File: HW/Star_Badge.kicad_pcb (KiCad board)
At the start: 2 copper layers, 180 x 171.6 mm, 55 parts, among them J1 AVR-ISP-6, J2 10118194-0001LF, Q1 Q_NMOS_DGS, Q2 Q_PMOS_DGS, U1 ATTINY861-15XD, U2 TPS613221ADBVT, U3 AP7363-33D-13, X1 Badgelife_sao_connector_v169b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, X2 Badgelife_sao_connector_v169b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, X3 Badgelife_sao_connector_v169b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

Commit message: update layout with new test points
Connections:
- TP3 pad 1: /R_LED_BUS -> /R_PWM__MISO
- TP4 pad 1: /G_LED_BUS -> /G_PWM
- TP5 pad 1: /B_LED_BUS -> /B_PWM
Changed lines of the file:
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@@
   )
   (setup
-    (last_trace_width 0.508)
+    (last_trace_width 0.1524)
     (user_trace_width 0.1524)
     (user_trace_width 0.2032)
@@
     )
     (pad 1 smd circle (at 0 0) (size 1 1) (layers B.Cu B.Mask)
-      (net 6 /R_LED_BUS))
+      (net 14 /R_PWM__MISO))
   )
   (module TestPoint:TestPoint_Pad_D1.0mm (layer B.Cu)
@@
     (fp_circle (center 0 0) (end 0 -0.7) (layer B.SilkS) (width 0.12))
     (pad 1 smd circle (at 0 0) (size 1 1) (layers B.Cu B.Mask)
-      (net 8 /G_LED_BUS))
+      (net 21 /G_PWM))
   )
   (module TestPoint:TestPoint_Pad_D1.0mm (layer B.Cu)
@@
     )
     (pad 1 smd circle (at 0 0) (size 1 1) (layers B.Cu B.Mask)
-      (net 9 /B_LED_BUS))
+      (net 22 /B_PWM))
   )
   (module TestPoint:TestPoint_Pad_D1.0mm (layer B.Cu)

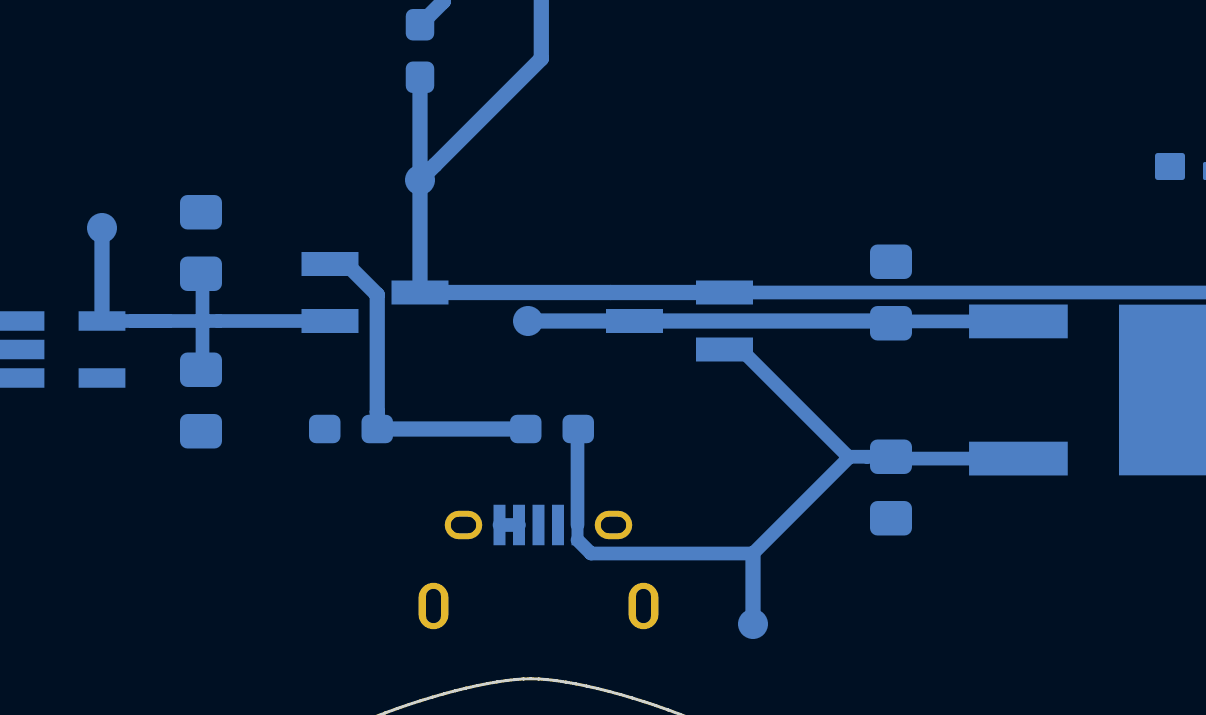
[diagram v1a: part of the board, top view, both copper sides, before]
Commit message: Spaced out parts
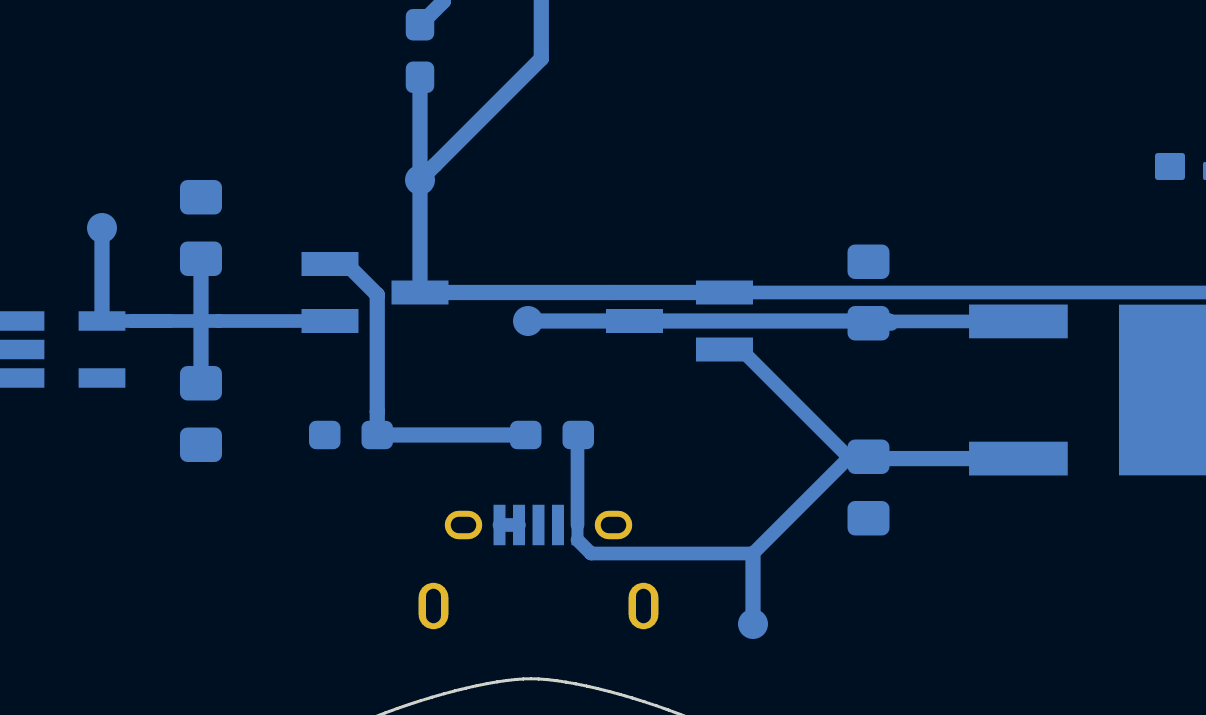
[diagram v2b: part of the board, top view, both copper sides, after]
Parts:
- moved C1 0.75 mm to (111.2, 154.2)
- moved C2 0.75 mm to (111.2, 147.8)
- moved C3 0.50 mm to (89.0, 145.6)
- moved C4 0.45 mm to (89.0, 151.8)
- moved R6 0.20 mm to (100.7, 152.5)
- moved R7 0.20 mm to (94.0, 152.5)
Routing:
- net /V_BAT: track 15.2 -> 16.2 mm
- net /V_USB: track 27.3 -> 28.0 mm
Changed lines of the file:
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@@
     (thickness 1.6)
     (drawings 611)
-    (tracks 62)
+    (tracks 58)
     (zones 0)
     (modules 55)
@@
   (page A4)
   (layers
-    (0 F.Cu signal)
+    (0 F.Cu signal hide)
     (31 B.Cu signal)
     (32 B.Adhes user hide)
@@
     (35 F.Paste user hide)
     (36 B.SilkS user)
-    (37 F.SilkS user)
+    (37 F.SilkS user hide)
     (38 B.Mask user)
     (39 F.Mask user hide)
@@
     (44 Edge.Cuts user)
     (45 Margin user hide)
-    (46 B.CrtYd user)
+    (46 B.CrtYd user hide)
     (47 F.CrtYd user hide)
     (48 B.Fab user hide)
@@
   )
   (setup
-    (last_trace_width 0.1524)
+    (last_trace_width 0.508)
     (user_trace_width 0.1524)
     (user_trace_width 0.2032)
@@
       (effects (font (size 1 1) (thickness 0.15)) (justify mirror))
     )
-    (fp_text value AP7363-33D-13 (at 1.289178 -6.901489 180) (layer B.SilkS) hide
+    (fp_text value AP7363-33D-13 (at -4.2 -0.1 180) (layer B.SilkS) hide
       (effects (font (size 1 1) (thickness 0.15)) (justify mirror))
     )
@@
   )
   (module Resistor_SMD:R_0603_1608Metric_Pad1.05x0.95mm_HandSolder (layer B.Cu)
-    (at 94 152.3)
+    (at 94 152.5)
     (descr "Resistor SMD 0603 (1608 Metric), square (rectangular) end terminal, IPC_7351 nominal with elongated pad for handsoldering. (Body size source: http://www.tortai-tech.com/upload/download/2011102023233369053.pdf), generated with kicad-footprint-generator")
     (tags "resistor handsolder")
@@
   )
   (module Resistor_SMD:R_0603_1608Metric_Pad1.05x0.95mm_HandSolder (layer B.Cu)
-    (at 100.7 152.3)
+    (at 100.7 152.5)
     (descr "Resistor SMD 0603 (1608 Metric), square (rectangular) end terminal, IPC_7351 nominal with elongated pad for handsoldering. (Body size source: http://www.tortai-tech.com/upload/download/2011102023233369053.pdf), generated with kicad-footprint-generator")
     (tags "resistor handsolder")
@@
   )
   (module Capacitor_SMD:C_0805_2012Metric_Pad1.15x1.40mm_HandSolder (layer B.Cu)
-    (at 89 151.35 270)
+    (at 89 151.8 270)
     (descr "Capacitor SMD 0805 (2012 Metric), square (rectangular) end terminal, IPC_7351 nominal with elongated pad for handsoldering. (Body size source: https://docs.google.com/spreadsheets/d/1BsfQQcO9C6DZCsRaXUlFlo91Tg2WpOkGARC1WS5S8t0/edit?usp=sharing), generated with kicad-footprint-generator")
     (tags "capacitor handsolder")
@@
   )
   (module Capacitor_SMD:C_0805_2012Metric_Pad1.15x1.40mm_HandSolder (layer B.Cu)
-    (at 89 146.1 90)
+    (at 89 145.6 90)
     (descr "Capacitor SMD 0805 (2012 Metric), square (rectangular) end terminal, IPC_7351 nominal with elongated pad for handsoldering. (Body size source: https://docs.google.com/spreadsheets/d/1BsfQQcO9C6DZCsRaXUlFlo91Tg2WpOkGARC1WS5S8t0/edit?usp=sharing), generated with kicad-footprint-generator")
     (tags "capacitor handsolder")
@@
   )
   (module Capacitor_SMD:C_0805_2012Metric_Pad1.15x1.40mm_HandSolder (layer B.Cu)
-    (at 112 147.75 90)
+    (at 111.25 147.75 90)
     (descr "Capacitor SMD 0805 (2012 Metric), square (rectangular) end terminal, IPC_7351 nominal with elongated pad for handsoldering. (Body size source: https://docs.google.com/spreadsheets/d/1BsfQQcO9C6DZCsRaXUlFlo91Tg2WpOkGARC1WS5S8t0/edit?usp=sharing), generated with kicad-footprint-generator")
     (tags "capacitor handsolder")
@@
   )
   (module Capacitor_SMD:C_0805_2012Metric_Pad1.15x1.40mm_HandSolder (layer B.Cu)
-    (at 112 154.25 270)
+    (at 111.25 154.25 270)
     (descr "Capacitor SMD 0805 (2012 Metric), square (rectangular) end terminal, IPC_7351 nominal with elongated pad for handsoldering. (Body size source: https://docs.google.com/spreadsheets/d/1BsfQQcO9C6DZCsRaXUlFlo91Tg2WpOkGARC1WS5S8t0/edit?usp=sharing), generated with kicad-footprint-generator")
     (tags "capacitor handsolder")
@@
   (gr_line (start 100.038258 14.223787) (end 100.038258 14.223787) (layer Edge.Cuts) (width 0.1))
   (segment (start 99.6 155.5) (end 98.95 155.5) (width 0.4572) (layer B.Cu) (net 1))
-  (segment (start 89.075 152.3) (end 89 152.375) (width 0.508) (layer B.Cu) (net 1))
   (segment (start 72.85 116.475) (end 66.6 124.1822) (width 0.4572) (layer B.Cu) (net 2))
   (segment (start 79.05 148.5) (end 79.2 148.65) (width 0.4572) (layer B.Cu) (net 2))
@@
   (segment (start 73.2 148.55) (end 73.2 151.5) (width 0.508) (layer B.Cu) (net 2))
   (segment (start 73.25 148.5) (end 73.2 148.55) (width 0.508) (layer B.Cu) (net 2))
-  (segment (start 112.211 153.286) (end 112.15 153.225) (width 0.4572) (layer B.Cu) (net 3))
-  (segment (start 116.2468 153.286) (end 112.211 153.286) (width 0.4572) (layer B.Cu) (net 3))
-  (segment (start 111.2 153.225) (end 112 153.225) (width 0.4572) (layer B.Cu) (net 3))
   (segment (start 107.4 156.45) (end 110.625 153.225) (width 0.4572) (layer B.Cu) (net 3))
   (segment (start 101.55 156) (end 102 156.45) (width 0.4572) (layer B.Cu) (net 3))
@@
   (segment (start 110.625 153.225) (end 110.575 153.225) (width 0.4572) (layer B.Cu) (net 3))
   (segment (start 107.4 158.8) (end 107.4 156.45) (width 0.508) (layer B.Cu) (net 3))
+  (segment (start 110.686 153.286) (end 110.625 153.225) (width 0.508) (layer B.Cu) (net 3))
+  (segment (start 116.2468 153.286) (end 110.686 153.286) (width 0.508) (layer B.Cu) (net 3))
   (segment (start 112.011 148.714) (end 112 148.725) (width 0.4572) (layer B.Cu) (net 4))
   (segment (start 116.2468 148.714) (end 112.011 148.714) (width 0.4572) (layer B.Cu) (net 4))
@@
   (segment (start 89.5872 148.7) (end 93.3 148.7) (width 0.4572) (layer B.Cu) (net 5))
   (segment (start 86.7 148.7) (end 87.9372 148.7) (width 0.4572) (layer B.Cu) (net 5))
-  (segment (start 89 150.275) (end 89.05 150.325) (width 0.4572) (layer B.Cu) (net 5))
-  (segment (start 89.05 148.65) (end 89.05 147.125) (width 0.4572) (layer B.Cu) (net 5))
   (segment (start 89.05 148.7) (end 89 148.65) (width 0.4572) (layer B.Cu) (net 5))
   (segment (start 89.5872 148.7) (end 89.05 148.7) (width 0.4572) (layer B.Cu) (net 5))
   (segment (start 89.05 148.7) (end 85.7 148.7) (width 0.4572) (layer B.Cu) (net 5))
-  (segment (start 89.05 148.7) (end 89.05 150.325) (width 0.4572) (layer B.Cu) (net 5))
   (segment (start 85.7 148.7) (end 85.7 145.6) (width 0.508) (layer B.Cu) (net 5))
+  (segment (start 89 150.775) (end 89 146.625) (width 0.508) (layer B.Cu) (net 5))
   (segment (start 102.6572 147.75) (end 106.45 147.75) (width 0.508) (layer B.Cu) (net 15))
   (segment (start 102.6572 147.75) (end 96.3 147.75) (width 0.508) (layer B.Cu) (net 15))
@@
   (segment (start 83 150.6) (end 79.225 150.6) (width 0.4572) (layer B.Cu) (net 19))
   (segment (start 93.3 146.8) (end 93.314198 146.8) (width 0.4572) (layer B.Cu) (net 20))
-  (segment (start 94.875 152.3) (end 99.825 152.3) (width 0.508) (layer B.Cu) (net 20))
+  (segment (start 94.875 152.5) (end 99.825 152.5) (width 0.508) (layer B.Cu) (net 20))
   (segment (start 94.875 147.825) (end 94.875 151.725) (width 0.508) (layer B.Cu) (net 20))
   (segment (start 93.85 146.8) (end 94.875 147.825) (width 0.508) (layer B.Cu) (net 20))

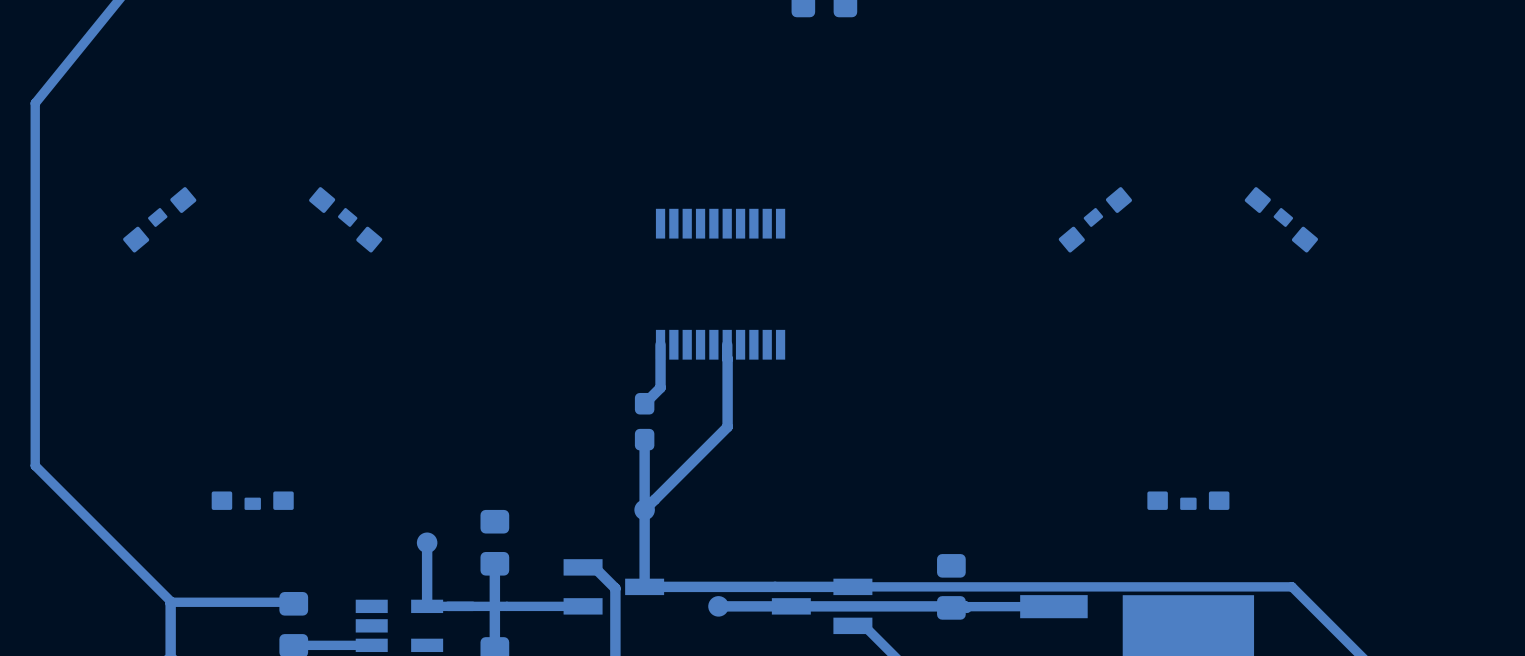
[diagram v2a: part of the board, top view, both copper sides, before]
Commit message: Routing - net around star 3. Adjusted R G LED to route.
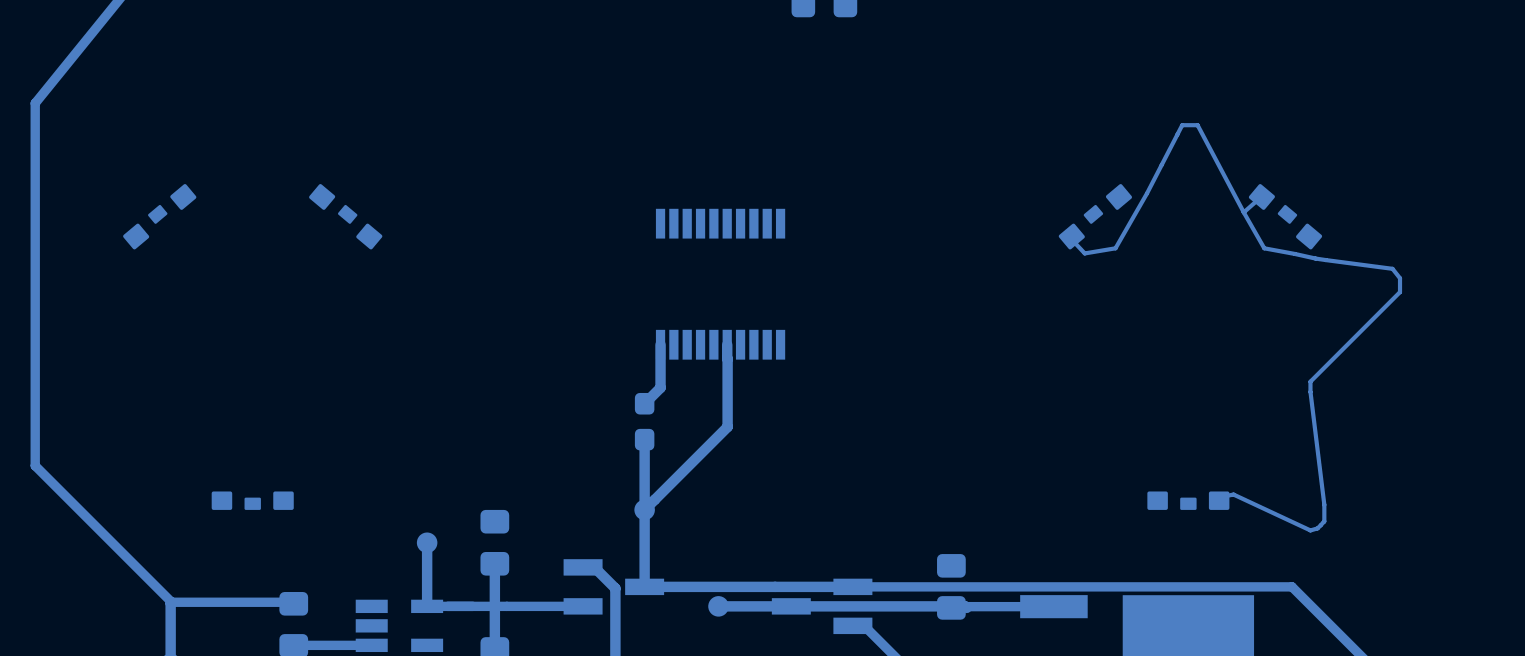
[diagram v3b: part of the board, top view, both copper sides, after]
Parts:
- moved D10 0.25 mm to (127.5, 129.8)
- moved D11 0.15 mm to (118.3, 129.8)
- moved D7 0.15 mm to (81.7, 129.8)
- moved D8 0.15 mm to (72.7, 129.8)
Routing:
- net /EN_RGB3: track 0.00 -> 44.1 mm
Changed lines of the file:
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@@
     (thickness 1.6)
     (drawings 611)
-    (tracks 58)
+    (tracks 85)
     (zones 0)
     (modules 55)
@@
     (32 B.Adhes user hide)
     (33 F.Adhes user hide)
-    (34 B.Paste user)
+    (34 B.Paste user hide)
     (35 F.Paste user hide)
     (36 B.SilkS user)
@@
   )
   (setup
-    (last_trace_width 0.508)
+    (last_trace_width 0.2032)
     (user_trace_width 0.1524)
     (user_trace_width 0.2032)
@@
   )
   (module Star_Badge:1204_SIDE_VIEW_LED locked (layer B.Cu)
-    (at 118.3 129.9 40)
+    (at 118.3 129.75 40)
     (fp_text reference D11 (at -0.031676 -1.984691 40) (layer B.SilkS)
       (effects (font (size 0.7 0.7) (thickness 0.15)) (justify mirror))
@@
   )
   (module Star_Badge:1204_SIDE_VIEW_LED locked (layer B.Cu)
-    (at 127.3 129.9 320)
+    (at 127.5 129.75 320)
     (fp_text reference D10 (at 0.044002 -2.125574 320) (layer B.SilkS)
       (effects (font (size 0.7 0.7) (thickness 0.15)) (justify mirror))
@@
     )
   )
-  (module Star_Badge:1204_SIDE_VIEW_LED (layer B.Cu)
-    (at 72.7 129.9 40)
+  (module Star_Badge:1204_SIDE_VIEW_LED locked (layer B.Cu)
+    (at 72.7 129.75 40)
     (fp_text reference D8 (at 0.084555 -2.278783 40) (layer B.SilkS)
       (effects (font (size 0.7 0.7) (thickness 0.15)) (justify mirror))
@@
     )
   )
-  (module Star_Badge:1204_SIDE_VIEW_LED (layer B.Cu)
-    (at 81.7 129.9 320)
+  (module Star_Badge:1204_SIDE_VIEW_LED locked (layer B.Cu)
+    (at 81.7 129.75 320)
     (fp_text reference D7 (at 0.044002 -2.125574 320) (layer B.SilkS)
       (effects (font (size 0.7 0.7) (thickness 0.15)) (justify mirror))
@@
   (segment (start 85.7 148.7) (end 85.7 145.6) (width 0.508) (layer B.Cu) (net 5))
   (segment (start 89 150.775) (end 89 146.625) (width 0.508) (layer B.Cu) (net 5))
+  (segment (start 119.25 131.25) (end 117.75 131.5) (width 0.2032) (layer B.Cu) (net 12))
+  (segment (start 121.5 127.186948) (end 120.78461 128.573568) (width 0.2032) (layer B.Cu) (net 12))
+  (segment (start 117.75 131.5) (end 117.118794 130.825879) (width 0.2032) (layer B.Cu) (net 12))
+  (segment (start 120.78461 128.573568) (end 119.25 131.25) (width 0.2032) (layer B.Cu) (net 12))
+  (segment (start 125.5 129.5) (end 123.25 125.25) (width 0.2032) (layer B.Cu) (net 12))
+  (segment (start 126.183073 128.897516) (end 125.5 129.5) (width 0.2032) (layer B.Cu) (net 12))
+  (segment (start 123.25 125.25) (end 122.5 125.25) (width 0.2032) (layer B.Cu) (net 12))
+  (segment (start 122.5 125.25) (end 122.265495 125.706063) (width 0.2032) (layer B.Cu) (net 12))
+  (segment (start 122.265495 125.706063) (end 121.5 127.186948) (width 0.2032) (layer B.Cu) (net 12))
+  (segment (start 128 131.526442) (end 126.5 131.25) (width 0.2032) (layer B.Cu) (net 12))
+  (segment (start 129 131.75) (end 128 131.526442) (width 0.2032) (layer B.Cu) (net 12))
+  (segment (start 129.5 131.82345) (end 129 131.75) (width 0.2032) (layer B.Cu) (net 12))
+  (segment (start 132.75 132.25) (end 129.5 131.82345) (width 0.2032) (layer B.Cu) (net 12))
+  (segment (start 133.11379 132.708844) (end 132.75 132.25) (width 0.2032) (layer B.Cu) (net 12))
+  (segment (start 125 143.25) (end 128.75 145) (width 0.2032) (layer B.Cu) (net 12))
+  (segment (start 126.5 131.25) (end 125.5 129.5) (width 0.2032) (layer B.Cu) (net 12))
+  (segment (start 129.42571 144.560096) (end 129.42571 143.75) (width 0.2032) (layer B.Cu) (net 12))
+  (segment (start 129.25 144.75) (end 129.39777 144.588036) (width 0.2032) (layer B.Cu) (net 12))
+  (segment (start 129.099116 144.89939) (end 129.25 144.75) (width 0.2032) (layer B.Cu) (net 12))
+  (segment (start 124.3 143.55) (end 124.5 143.35) (width 0.2032) (layer B.Cu) (net 12))
+  (segment (start 133.11379 133.38621) (end 133.11379 132.708844) (width 0.2032) (layer B.Cu) (net 12))
+  (segment (start 128.75 137.75) (end 133.11379 133.38621) (width 0.2032) (layer B.Cu) (net 12))
+  (segment (start 124.5 143.35) (end 125 143.25) (width 0.2032) (layer B.Cu) (net 12))
+  (segment (start 128.75 145) (end 129.099116 144.89939) (width 0.2032) (layer B.Cu) (net 12))
+  (segment (start 129.42571 143.75) (end 128.75 138.25) (width 0.2032) (layer B.Cu) (net 12))
+  (segment (start 128.75 138.25) (end 128.75 137.75) (width 0.2032) (layer B.Cu) (net 12))
+  (segment (start 129.39777 144.588036) (end 129.42571 144.560096) (width 0.2032) (layer B.Cu) (net 12))
   (segment (start 102.6572 147.75) (end 106.45 147.75) (width 0.508) (layer B.Cu) (net 15))
   (segment (start 102.6572 147.75) (end 96.3 147.75) (width 0.508) (layer B.Cu) (net 15))
@@
     (connect_pads (clearance 0.254))
     (min_thickness 0.254)
-    (fill yes (arc_segments 32) (thermal_gap 0.508) (thermal_bridge_width 0.508))
+    (fill yes (arc_segments 32) (thermal_gap 0.45) (thermal_bridge_width 0.45))
     (polygon
       (pts
